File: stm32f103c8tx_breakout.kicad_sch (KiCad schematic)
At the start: 33 parts, among them J1 USB_B_Micro, J2 Conn_02x05_Odd_Even, J3 Conn_01x12, J4 Conn_01x07, J5 Conn_01x12, J6 Conn_01x06, SW1 SW_SPDT, U1 AMS1117-3.3, U2 STM32F103C8T6, Y1 16M

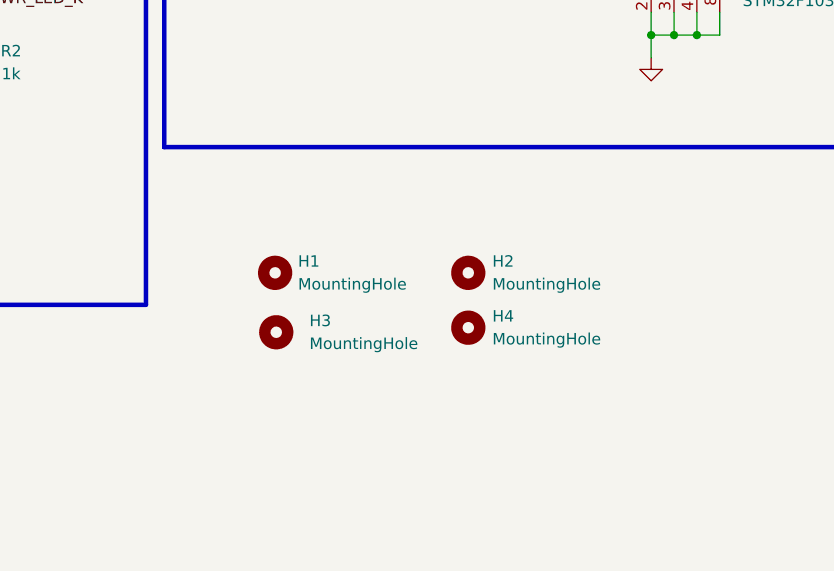
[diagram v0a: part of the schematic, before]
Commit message: Changes to fix for jlcpcb parts
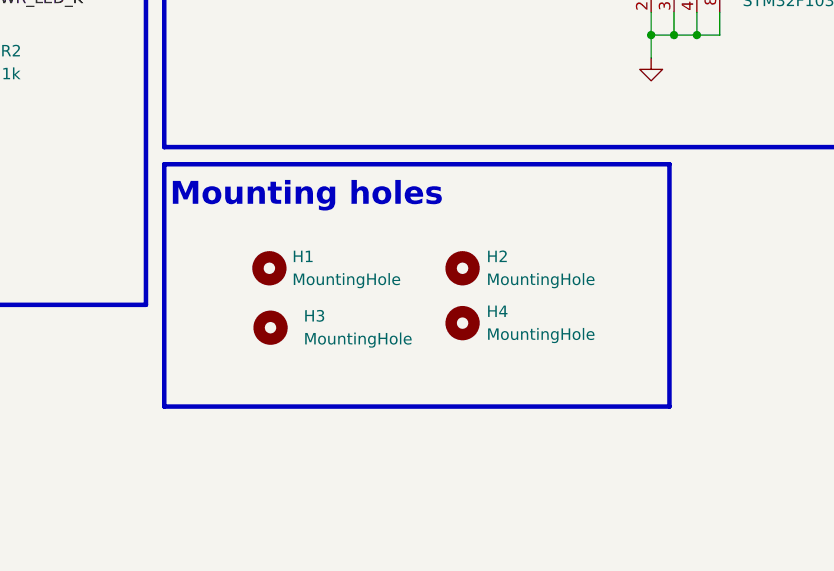
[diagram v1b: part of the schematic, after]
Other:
- note added: "Mounting holes"
- moved on the sheet: H1, H2, H3, H4
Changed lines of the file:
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@@
     (stroke (width 0) (type default) (color 0 0 0 0))
+  )
+  (polyline (pts (xy 142.875 139.065) (xy 142.875 165.989))
+    (stroke (width 0.5) (type solid) (color 0 0 0 0))
   )
   (wire (pts (xy 39.751 82.804) (xy 39.751 85.344))
@@
   (wire (pts (xy 97.028 35.814) (xy 97.028 37.084))
     (stroke (width 0) (type default) (color 0 0 0 0))
+  )
+  (polyline (pts (xy 86.741 139.065) (xy 142.875 139.065))
+    (stroke (width 0.5) (type solid) (color 0 0 0 0))
   )
   (wire (pts (xy 223.139 37.465) (xy 223.139 34.925))
@@
     (stroke (width 0) (type default) (color 0 0 0 0))
   )
+  (polyline (pts (xy 142.875 165.989) (xy 86.741 165.989))
+    (stroke (width 0.5) (type solid) (color 0 0 0 0))
+  )
   (wire (pts (xy 216.789 40.005) (xy 220.599 40.005))
     (stroke (width 0) (type default) (color 0 0 0 0))
@@
   (wire (pts (xy 156.083 35.814) (xy 164.973 35.814))
     (stroke (width 0) (type default) (color 0 0 0 0))
+  )
+  (polyline (pts (xy 86.741 139.065) (xy 86.741 165.989))
+    (stroke (width 0.5) (type solid) (color 0 0 0 0))
   )
   (wire (pts (xy 104.648 35.814) (xy 113.538 35.814))
@@
     (effects (font (size 6.35 6.35) (thickness 1.27) bold) (justify left bottom))
   )
+  (text "Mounting holes\n" (at 87.376 144.018 0)
+    (effects (font (size 2.54 2.54) (thickness 0.508) bold) (justify left bottom))
+  )
   (text "100nF per power pin, 10u bulk capacitor" (at 92.837 32.512 0)
     (effects (font (size 1.27 1.27)) (justify left bottom))
@@
     (pin "1")
   )
-  (symbol (lib_id "Mechanical:MountingHole") (at 120.523 151.13 0) (unit 1)
+  (symbol (lib_id "Mechanical:MountingHole") (at 119.888 150.622 0) (unit 1)
     (in_bom yes) (on_board yes) (fields_autoplaced)
-    (property "Reference" "H2" (id 0) (at 123.19 149.8599 0)
-      (effects (font (size 1.27 1.27)) (justify left))
-    )
-    (property "Value" "MountingHole" (id 1) (at 123.19 152.3999 0)
-      (effects (font (size 1.27 1.27)) (justify left))
-    )
-    (property "Footprint" "MountingHole:MountingHole_3.2mm_M3" (id 2) (at 120.523 151.13 0)
-      (effects (font (size 1.27 1.27)) hide)
-    )
-    (property "Datasheet" "~" (id 3) (at 120.523 151.13 0)
+    (property "Reference" "H2" (id 0) (at 122.555 149.3519 0)
+      (effects (font (size 1.27 1.27)) (justify left))
+    )
+    (property "Value" "MountingHole" (id 1) (at 122.555 151.8919 0)
+      (effects (font (size 1.27 1.27)) (justify left))
+    )
+    (property "Footprint" "MountingHole:MountingHole_3.2mm_M3" (id 2) (at 119.888 150.622 0)
+      (effects (font (size 1.27 1.27)) hide)
+    )
+    (property "Datasheet" "~" (id 3) (at 119.888 150.622 0)
       (effects (font (size 1.27 1.27)) hide)
     )
@@
     (pin "9")
   )
-  (symbol (lib_id "Mechanical:MountingHole") (at 99.187 157.734 0) (unit 1)
+  (symbol (lib_id "Mechanical:MountingHole") (at 98.552 157.226 0) (unit 1)
     (in_bom yes) (on_board yes) (fields_autoplaced)
-    (property "Reference" "H3" (id 0) (at 102.87 156.4639 0)
-      (effects (font (size 1.27 1.27)) (justify left))
-    )
-    (property "Value" "MountingHole" (id 1) (at 102.87 159.0039 0)
-      (effects (font (size 1.27 1.27)) (justify left))
-    )
-    (property "Footprint" "MountingHole:MountingHole_3.2mm_M3" (id 2) (at 99.187 157.734 0)
-      (effects (font (size 1.27 1.27)) hide)
-    )
-    (property "Datasheet" "~" (id 3) (at 99.187 157.734 0)
+    (property "Reference" "H3" (id 0) (at 102.235 155.9559 0)
+      (effects (font (size 1.27 1.27)) (justify left))
+    )
+    (property "Value" "MountingHole" (id 1) (at 102.235 158.4959 0)
+      (effects (font (size 1.27 1.27)) (justify left))
+    )
+    (property "Footprint" "MountingHole:MountingHole_3.2mm_M3" (id 2) (at 98.552 157.226 0)
+      (effects (font (size 1.27 1.27)) hide)
+    )
+    (property "Datasheet" "~" (id 3) (at 98.552 157.226 0)
       (effects (font (size 1.27 1.27)) hide)
     )
@@
     (pin "2")
   )
-  (symbol (lib_id "Mechanical:MountingHole") (at 99.06 151.13 0) (unit 1)
+  (symbol (lib_id "Mechanical:MountingHole") (at 98.425 150.622 0) (unit 1)
     (in_bom yes) (on_board yes) (fields_autoplaced)
-    (property "Reference" "H1" (id 0) (at 101.6 149.8599 0)
-      (effects (font (size 1.27 1.27)) (justify left))
-    )
-    (property "Value" "MountingHole" (id 1) (at 101.6 152.3999 0)
-      (effects (font (size 1.27 1.27)) (justify left))
-    )
-    (property "Footprint" "MountingHole:MountingHole_3.2mm_M3" (id 2) (at 99.06 151.13 0)
-      (effects (font (size 1.27 1.27)) hide)
-    )
-    (property "Datasheet" "~" (id 3) (at 99.06 151.13 0)
+    (property "Reference" "H1" (id 0) (at 100.965 149.3519 0)
+      (effects (font (size 1.27 1.27)) (justify left))
+    )
+    (property "Value" "MountingHole" (id 1) (at 100.965 151.8919 0)
+      (effects (font (size 1.27 1.27)) (justify left))
+    )
+    (property "Footprint" "MountingHole:MountingHole_3.2mm_M3" (id 2) (at 98.425 150.622 0)
+      (effects (font (size 1.27 1.27)) hide)
+    )
+    (property "Datasheet" "~" (id 3) (at 98.425 150.622 0)
       (effects (font (size 1.27 1.27)) hide)
     )
@@
     (pin "6")
   )
-  (symbol (lib_id "Mechanical:MountingHole") (at 120.523 157.226 0) (unit 1)
+  (symbol (lib_id "Mechanical:MountingHole") (at 119.888 156.718 0) (unit 1)
     (in_bom yes) (on_board yes) (fields_autoplaced)
-    (property "Reference" "H4" (id 0) (at 123.19 155.9559 0)
-      (effects (font (size 1.27 1.27)) (justify left))
-    )
-    (property "Value" "MountingHole" (id 1) (at 123.19 158.4959 0)
-      (effects (font (size 1.27 1.27)) (justify left))
-    )
-    (property "Footprint" "MountingHole:MountingHole_3.2mm_M3" (id 2) (at 120.523 157.226 0)
-      (effects (font (size 1.27 1.27)) hide)
-    )
-    (property "Datasheet" "~" (id 3) (at 120.523 157.226 0)
-      (effects (font (size 1.27 1.27)) hide)
-    )
+    (property "Reference" "H4" (id 0) (at 122.555 155.4479 0)
+      (effects (font (size 1.27 1.27)) (justify left))
+    )
+    (property "Value" "MountingHole" (id 1) (at 122.555 157.9879 0)
+      (effects (font (size 1.27 1.27)) (justify left))
+    )
+    (property "Footprint" "MountingHole:MountingHole_3.2mm_M3" (id 2) (at 119.888 156.718 0)
+      (effects (font (size 1.27 1.27)) hide)
+    )
+    (property "Datasheet" "~" (id 3) (at 119.888 156.718 0)
+      (effects (font (size 1.27 1.27)) hide)
+    )
